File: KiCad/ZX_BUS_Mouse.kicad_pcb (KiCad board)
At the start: 2 copper layers, 99.1 x 40 mm, 31 parts, among them J1 X1A, J2 X1B, J3 UART, J4 Mini-DIN-6, J5 ISP, J6 Debug, J7 JTAG, J8 PS/2 External Bracket, U1 ATmega8A-A, U2 EPM3032ALC44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

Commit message: V.1.1. Add PCB version label. Update README.MD.
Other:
- board text added: "V.1.1"
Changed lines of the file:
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@@
     (effects (font (size 1 0.8) (thickness 0.15)) (justify mirror))
+  )
+  (gr_text "V.1.1" (at 49 137.9) (layer "B.SilkS")
+    (effects (font (size 1 1) (thickness 0.15)) (justify left bottom mirror))
   )
   (gr_text "RS/" (at 92.075 139.065 90) (layer "B.SilkS")

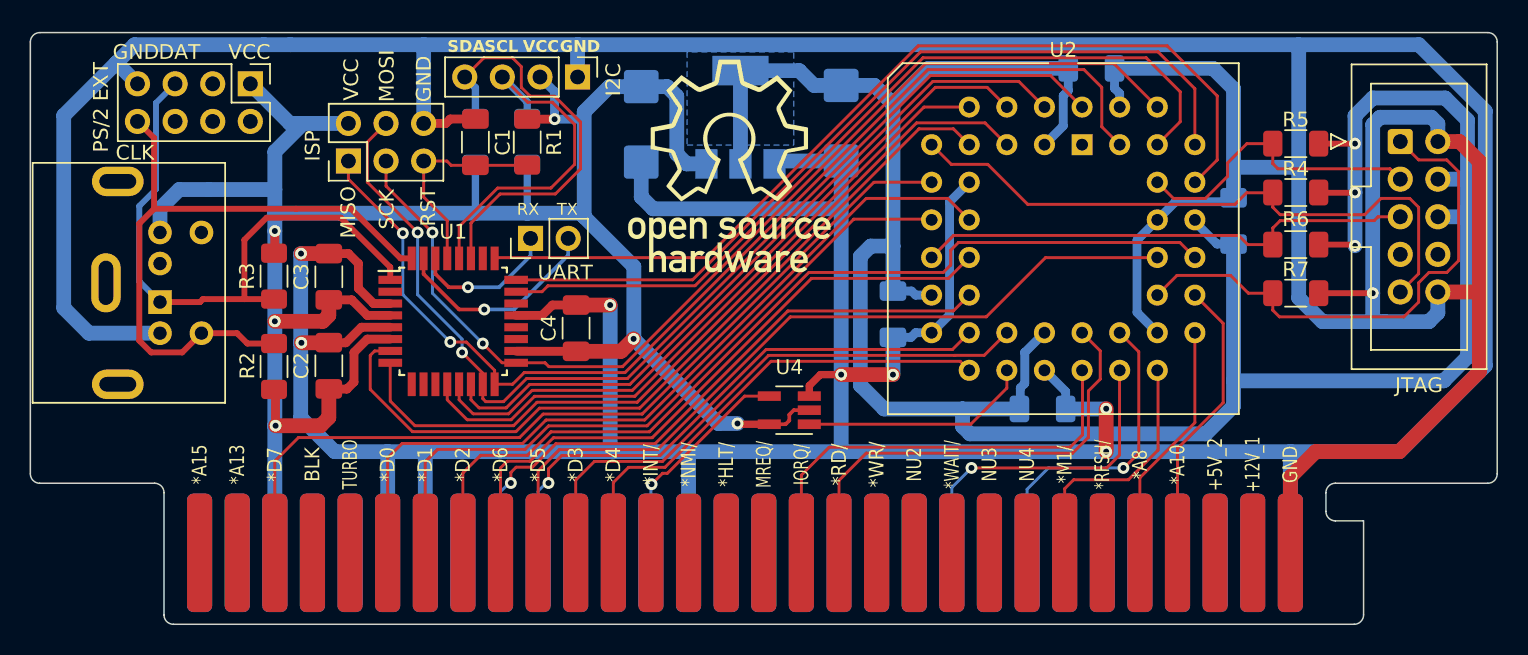
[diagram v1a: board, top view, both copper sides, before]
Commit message: Scorpion ZS 256 Service ROM / ProfROM by @LW_aka_PLM: fixed ROM Disk loading with mouse enabled. Added A15 to IORQGE / ports addresses decode.
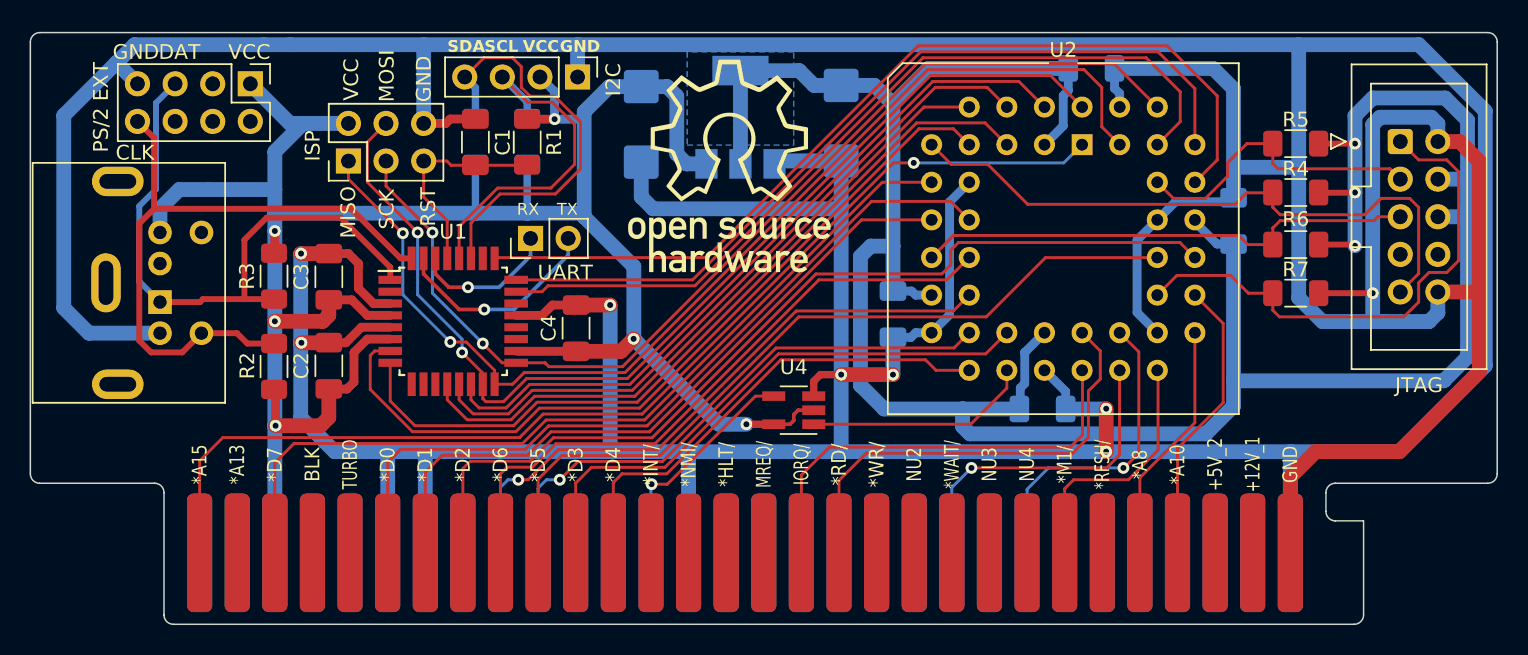
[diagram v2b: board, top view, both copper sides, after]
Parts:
- moved U4 0.30 mm to (94.1, 135.4)
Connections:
- U2 pad 1: unconnected-(U2A-~{GCLR}-Pad1) -> /*A15
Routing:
- net /*A15: track 0.00 -> 74.7 mm, vias 0 -> 1
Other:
- board text added: "V.1.2"
- board text removed: "V.1.1"
